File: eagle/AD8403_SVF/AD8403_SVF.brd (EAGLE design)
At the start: 100 x 80 mm, 21 parts, among them IC1 AD8403-DIP28, IC2 NJM2732, IC3 NJM2732

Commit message: Update: eagle files
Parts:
- added C10: 2.2uF, rcl:C050-055X075
- added JP7: VGND, pinhead:1X02
- added LED1, LED2: red, led:LED3MM
- added R4: 100k, rcl:0207/7
- added R5: 10k, pot:B25P
- added R6: 2.2k, rcl:0207/7
- added R7, R8: 220, rcl:0207/7
- C1, C2: device rcl:C025-025X050 -> rcl:C050-025X075
- C7: value (none) -> 0.1uF
- IC1: value AD8403-DIP28 -> AD8403-DIP24; device mylib2:AD8403-DIP28 -> mylib2:AD8403_DIP24
- JP2: value (none) -> PWR
- JP4: value LPFOUT -> LP
- JP5: value BPFOUT -> BP
- JP6: value HPFOUT -> HP
- moved C6 138.7 mm to (66.0, 26.7), turned to 90 degrees
- moved C8 134.8 mm to (62.2, 17.8), turned to 180 degrees
- moved C9 132.5 mm to (54.6, 17.8), turned to 180 degrees
- moved C5 127.6 mm to (53.3, 31.8), turned to 90 degrees
- moved JP5 121.1 mm to (54.6, 40.6)
- moved JP2 120.1 mm to (55.9, 5.08), turned to 180 degrees
- moved C7 118.5 mm to (45.7, 16.5), turned to 90 degrees
- moved JP6 117.7 mm to (47.0, 40.6)
- moved C2 109.7 mm to (58.4, 22.9)
- moved C3 85.2 mm to (20.3, 14.0), turned to 90 degrees
- moved C4 78.2 mm to (7.62, 16.5), turned to 90 degrees
- moved JP3 59.5 mm to (14.0, 40.6)
- moved R2 56.9 mm to (16.5, 22.9)
- moved R3 50.6 mm to (16.5, 25.4)
- moved IC2 48.2 mm to (14.0, 14.0)
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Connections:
- removed net +2V5: JP2.2
- new net N$11: C10.2, R1.1, R4.2
- new net N$12: IC1.2, R6.1
- new net N$14: LED2.K, R8.2
- new net N$15: LED1.K, R7.2
- new net N$2: C10.1, R5.S
- net +5V: now also LED1.A
- net GND: now also R5.A, R8.1; no longer IC3.5, JP4.2, JP5.2, JP6.2
- net N$1: now also R5.E; no longer R1.1
- net N$10: now also IC3.1, R6.2; no longer IC1.2, IC2.7
- net N$6: now also IC3.6; no longer IC3.2
- net N$7: now also IC3.2; no longer IC2.6
- net N$8: now also IC2.6, IC2.7; no longer IC3.6, IC3.7
- net N$9: now also IC3.7; no longer IC3.1
- net VCC/2: now also IC3.5, JP2.2, JP4.2, JP5.2, JP6.2, JP7.1, JP7.2, LED2.A, R4.1, R7.1
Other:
- board size 100 x 80 mm -> 70.8 x 45.7 mm

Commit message: Update: eagle files
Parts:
- added JP8: GND, pinhead:1X02
- R7, R8: device rcl:0207/7 -> rcl:0204V
- moved R6 25.7 mm to (34.3, 53.3), turned to 0 degrees
- moved JP3 16.1 mm to (8.89, 55.9)
- moved JP6 16.1 mm to (41.9, 55.9), turned to 180 degrees
- moved JP5 15.5 mm to (52.1, 55.9), turned to 180 degrees
- moved JP4 15.2 mm to (62.2, 55.9), turned to 180 degrees
- moved R5 15.2 mm to (7.62, 50.8)
- moved R7 13.1 mm to (61.0, 14.0), turned to 270 degrees
- moved C2 13.0 mm to (55.9, 35.6)
- moved C5 13.0 mm to (50.8, 44.5)
- moved JP1 13.0 mm to (29.2, 7.62)
- moved C1 13.0 mm to (58.4, 48.3)
- moved C6 13.0 mm to (63.5, 39.4)
- moved IC3 13.0 mm to (57.1, 41.9)
- moved C10 12.7 mm to (15.2, 48.3), turned to 270 degrees
- moved LED1 10.9 mm to (61.0, 19.1), turned to 90 degrees
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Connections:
- removed net N$15: LED1.K, R7.2
- new net N$13: LED1.A, R7.1
- net +5V: now also R7.2; no longer LED1.A
- net GND: now also JP4.2, JP5.2, JP6.2, JP8.1, JP8.2
- net VCC/2: now also LED1.K; no longer JP4.2, JP5.2, JP6.2, R7.1
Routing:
- net GND: track 0.00 -> 286.1 mm, vias 0 -> 2
- net VCC/2: track 0.00 -> 183.5 mm, vias 0 -> 4
- net N$9: track 0.00 -> 104.8 mm, vias 0 -> 4
- net +5V: track 0.00 -> 87.4 mm
- net N$5: track 0.00 -> 58.4 mm, vias 0 -> 4
- net N$10: track 0.00 -> 51.9 mm, vias 0 -> 4
- net N$3: track 0.00 -> 30.5 mm, vias 0 -> 2
- net N$7: track 0.00 -> 30.5 mm, vias 0 -> 2
- net SCK: track 0.00 -> 25.4 mm
- net N$6: track 0.00 -> 20.3 mm, vias 0 -> 2
- net !CS: track 0.00 -> 15.2 mm
- net N$11: track 0.00 -> 13.3 mm
- net N$12: track 0.00 -> 12.7 mm, vias 0 -> 2
- net N$2: track 0.00 -> 10.2 mm
- net MOSI: track 0.00 -> 10.2 mm
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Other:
- board size 70.8 x 45.7 mm -> 70.8 x 94 mm

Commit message: Update: eagle files
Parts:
- moved JP8 4.02 mm to (22.9, 57.1), turned to 90 degrees
- moved JP7 2.54 mm to (11.4, 12.7)
- turned R7 to 90 degrees
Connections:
- net +5V: now also IC1.15, R7.1; no longer R7.2
- net GND: no longer IC1.15, JP4.2, JP5.2, JP6.2
- net N$13: now also R7.2; no longer R7.1
- net VCC/2: now also JP4.2, JP5.2, JP6.2
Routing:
- net VCC/2: track 183.5 -> 226.7 mm
- net GND: track 286.1 -> 258.2 mm
- net +5V: track 87.4 -> 93.5 mm

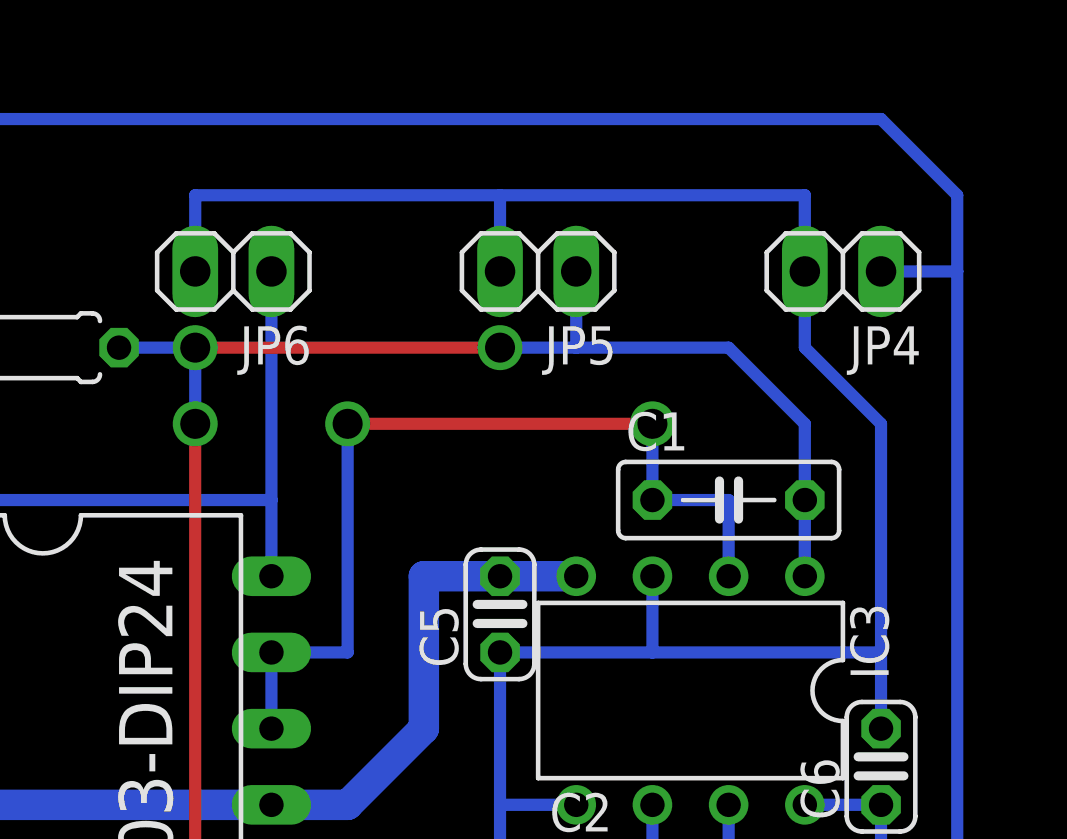
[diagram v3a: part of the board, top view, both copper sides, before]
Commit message: change the output GND from VGND to GND
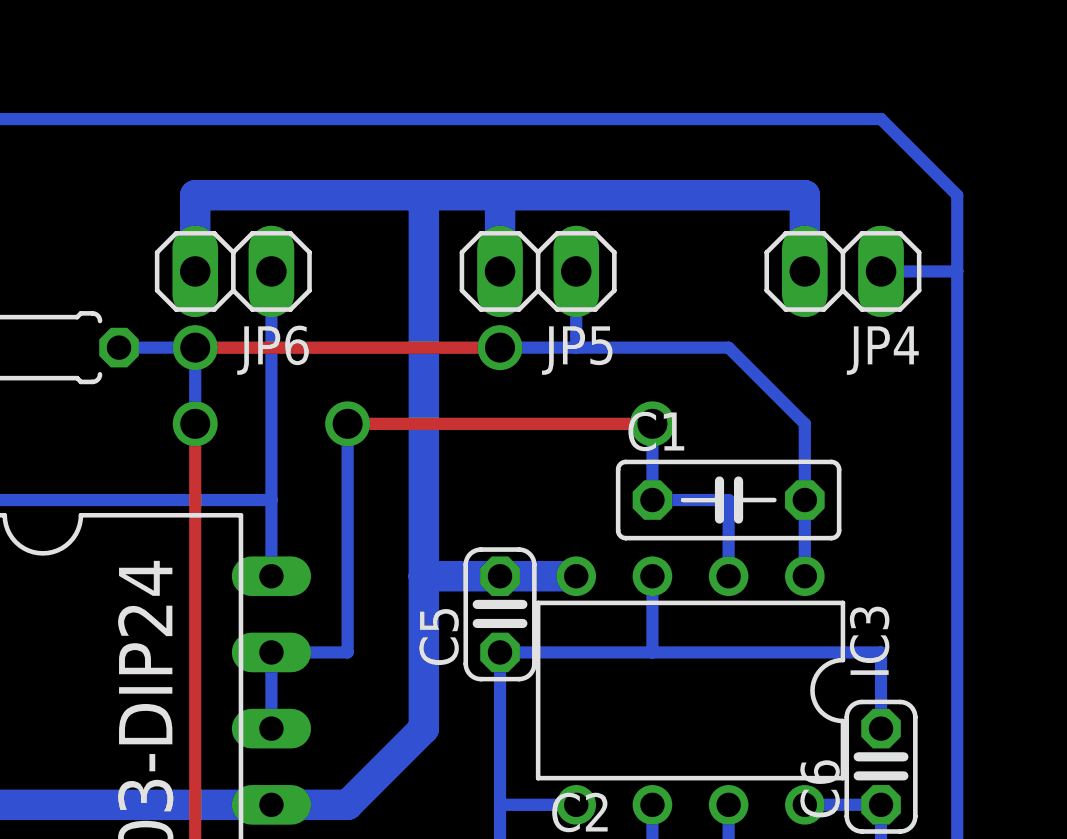
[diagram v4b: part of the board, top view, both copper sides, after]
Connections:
- net GND: now also JP4.2, JP5.2, JP6.2
- net VCC/2: no longer JP4.2, JP5.2, JP6.2
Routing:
- net VCC/2: track 226.7 -> 185.0 mm
- net GND: track 258.2 -> 298.8 mm
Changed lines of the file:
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@@
 <wire x1="45.72" y1="38.1" x2="48.26" y2="40.64" width="1.016" layer="16"/>
 <wire x1="48.26" y1="40.64" x2="48.26" y2="45.72" width="1.016" layer="16"/>
-<wire x1="48.26" y1="45.72" x2="50.8" y2="45.72" width="1.016" layer="16"/>
 <wire x1="22.86" y1="55.88" x2="22.86" y2="58.42" width="1.016" layer="16"/>
 <wire x1="43.18" y1="27.94" x2="40.64" y2="27.94" width="1.016" layer="16"/>
@@
 <wire x1="45.72" y1="5.08" x2="45.72" y2="15.24" width="1.016" layer="16"/>
 <wire x1="45.72" y1="15.24" x2="40.64" y2="15.24" width="1.016" layer="16"/>
+<contactref element="JP5" pad="2"/>
+<contactref element="JP4" pad="2"/>
+<contactref element="JP6" pad="2"/>
+<wire x1="40.64" y1="55.88" x2="40.64" y2="58.42" width="1.016" layer="16"/>
+<wire x1="40.64" y1="58.42" x2="48.26" y2="58.42" width="1.016" layer="16"/>
+<wire x1="48.26" y1="58.42" x2="50.8" y2="58.42" width="1.016" layer="16"/>
+<wire x1="50.8" y1="58.42" x2="60.96" y2="58.42" width="1.016" layer="16"/>
+<wire x1="60.96" y1="58.42" x2="60.96" y2="55.88" width="1.016" layer="16"/>
+<wire x1="50.8" y1="55.88" x2="50.8" y2="58.42" width="1.016" layer="16"/>
+<wire x1="50.8" y1="45.72" x2="48.26" y2="45.72" width="1.016" layer="16"/>
+<wire x1="48.26" y1="45.72" x2="48.26" y2="58.42" width="1.016" layer="16"/>
 </signal>
 <signal name="+5V">
@@
 <wire x1="10.16" y1="7.62" x2="7.62" y2="10.16" width="0.4064" layer="16"/>
 <wire x1="7.62" y1="10.16" x2="7.62" y2="12.7" width="0.4064" layer="16"/>
-<contactref element="JP6" pad="2"/>
-<contactref element="JP5" pad="2"/>
-<contactref element="JP4" pad="2"/>
-<wire x1="40.64" y1="55.88" x2="40.64" y2="58.42" width="0.4064" layer="16"/>
-<wire x1="40.64" y1="58.42" x2="50.8" y2="58.42" width="0.4064" layer="16"/>
-<wire x1="50.8" y1="58.42" x2="50.8" y2="55.88" width="0.4064" layer="16"/>
-<wire x1="60.96" y1="55.88" x2="60.96" y2="58.42" width="0.4064" layer="16"/>
-<wire x1="60.96" y1="58.42" x2="50.8" y2="58.42" width="0.4064" layer="16"/>
-<wire x1="60.96" y1="55.88" x2="60.96" y2="53.34" width="0.4064" layer="16"/>
-<wire x1="60.96" y1="53.34" x2="63.5" y2="50.8" width="0.4064" layer="16"/>
-<wire x1="63.5" y1="50.8" x2="63.5" y2="43.18" width="0.4064" layer="16"/>
 <wire x1="63.5" y1="43.18" x2="63.5" y2="40.64" width="0.4064" layer="16"/>
 </signal>
